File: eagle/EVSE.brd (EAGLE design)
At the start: 25.1 x 34.9 mm, 21 parts

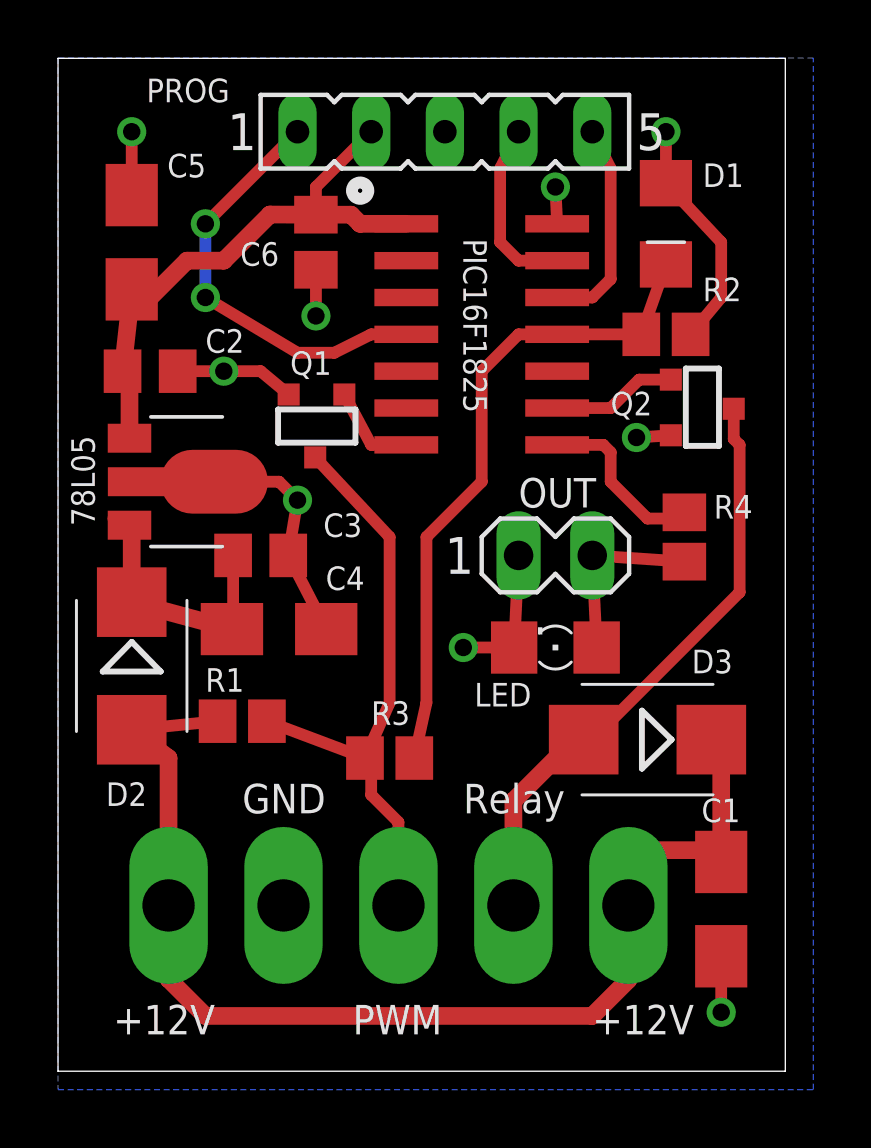
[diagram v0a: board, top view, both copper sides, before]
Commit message: Updated board layout - cosmetic changes.
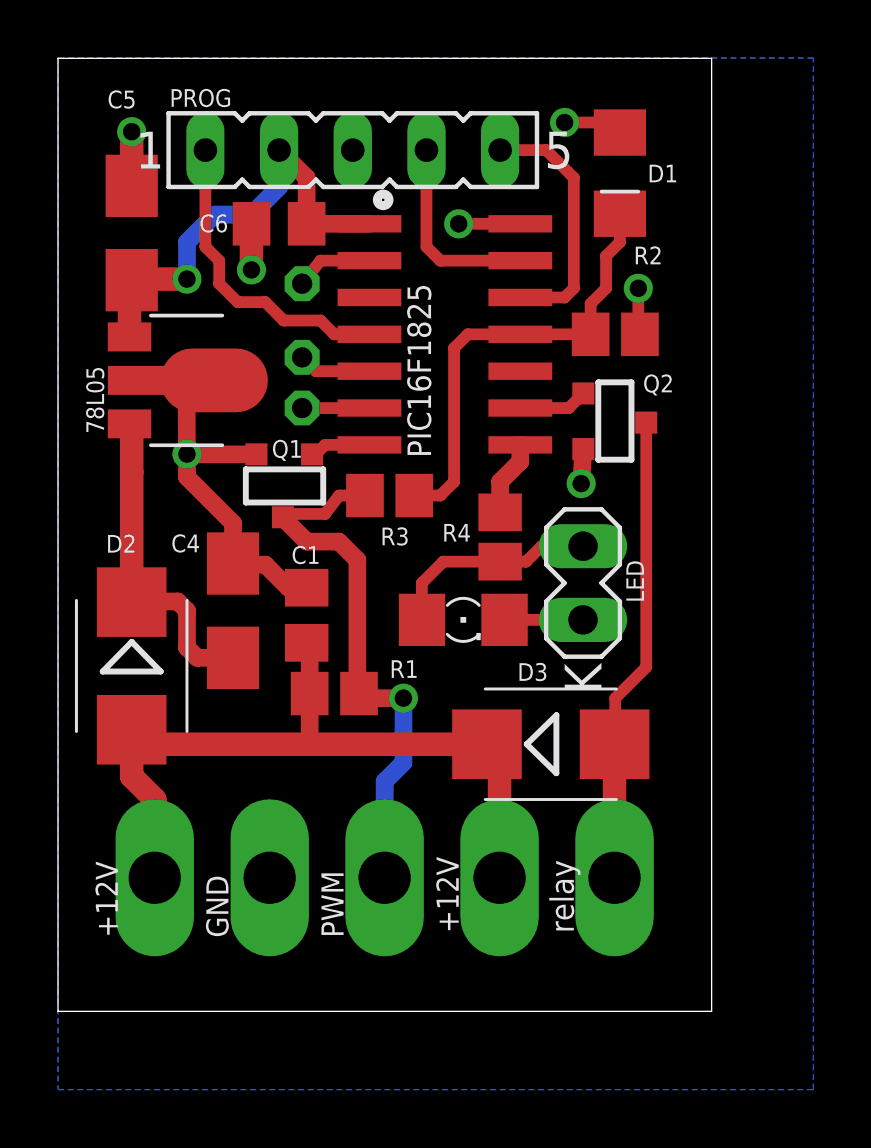
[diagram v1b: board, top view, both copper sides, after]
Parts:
- removed C2, C3: 100n, rcl:C0805
- removed OUT: MA02-1THT, superlibrary:MA02-1
- added LED_: (no value), led:1206
- added SV1, SV2, SV4: (no value), superlibrary:PIN-HEADER1
- C1: value 68u_6.3V -> 100n; device rcl:B/3528-21W -> rcl:C0805
- LED: value (none) -> MA02-1THT; device led:1206 -> superlibrary:MA02-1
- R2: value 5k -> 5k6
- moved C1 17.5 mm to (9.21, 17.0)
- moved R3 9.05 mm to (12.1, 21.1)
- moved R4 6.35 mm to (15.9, 19.7)
- moved LED 3.62 mm to (18.7, 19.4), turned to 90 degrees
- moved 78L05 3.49 mm to (5.08, 25.1)
- moved D3 3.34 mm to (17.6, 12.5), turned to 0 degrees
- moved R1 3.31 mm to (10.2, 14.3)
- moved PROG 3.24 mm to (10.8, 33.0)
- moved Q2 3.05 mm to (19.8, 23.7)
- moved D1 2.36 mm to (20.0, 32.2)
- moved Q1 2.34 mm to (8.41, 21.4)
- moved R2 1.75 mm to (19.8, 26.7)
- moved C4 1.71 mm to (6.67, 17.1), turned to 270 degrees
- moved C6 1.42 mm to (8.26, 30.5), turned to 180 degrees
- moved PIC16F1825 1.27 mm to (14.0, 26.7)
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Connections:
- new net N$5: PIC16F1825.2, SV1.1
- new net N$7: PIC16F1825.5, SV2.1
- new net N$8: PIC16F1825.6, SV4.1
- net +12V: now also C1.1, SV3.4; no longer C1.+, SV3.5
- net GND: now also C1.2, LED.1, LED_.C; no longer C1.-, C2.2, C3.2, LED.C, OUT.1
- net N$12: now also LED.2, LED_.A; no longer LED.A, OUT.2
- net N$2: no longer C3.1
- net REL: now also SV3.5; no longer SV3.4
- net VDD: no longer C2.1
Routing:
- net +12V: track 40.9 -> 26.2 mm
- net GND: track 35.9 -> 28.6 mm, vias 9 -> 7
- net N$3: track 22.8 -> 15.7 mm
- net REL: track 21.2 -> 16.1 mm
- net VDD: track 20.4 -> 15.5 mm, vias 0 -> 1
- net VPP: track 14.6 -> 10.7 mm, vias 2 -> 0
- net N$11: track 6.12 -> 2.61 mm
- net N$5: track 0.00 -> 2.70 mm
- net N$7: track 0.00 -> 2.52 mm
- net N$8: track 0.00 -> 2.32 mm
- net N$6: track 4.32 -> 2.38 mm
- net N$2: track 9.44 -> 11.2 mm
- net PWM: track 20.7 -> 19.1 mm, vias 0 -> 1
- net CLK: track 7.34 -> 8.72 mm
- net N$4: track 3.18 -> 2.11 mm
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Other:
- board size 25.1 x 34.9 mm -> 22.5 x 32.9 mm
- board text added: "relay"
- board text removed: "Relay"
